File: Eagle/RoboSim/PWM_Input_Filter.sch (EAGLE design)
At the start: 68 parts, among them IC1 LM358, IC2 LM358, IC3 LM358

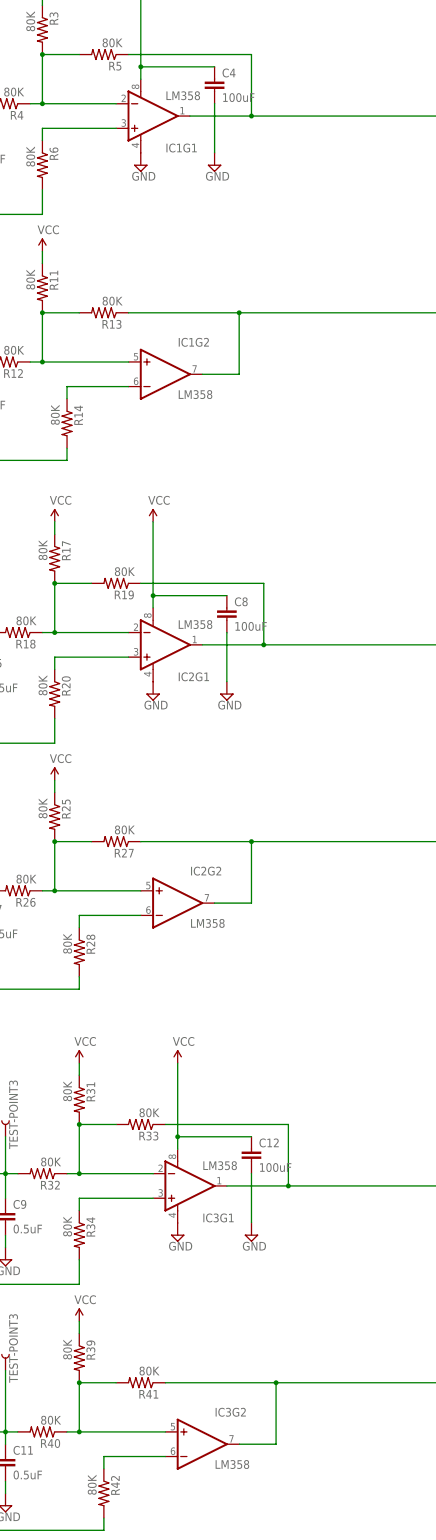
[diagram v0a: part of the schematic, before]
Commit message: updated op amp part number
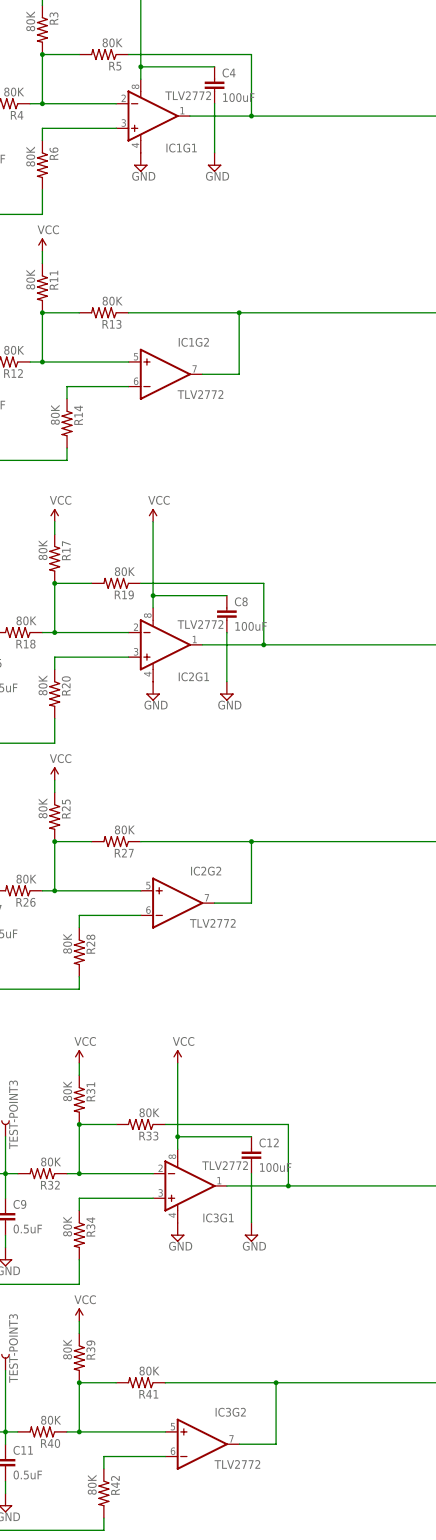
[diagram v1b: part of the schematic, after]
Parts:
- IC1, IC2, IC3: value LM358 -> TLV2772
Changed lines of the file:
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@@
 </classes>
 <parts>
-<part name="IC1" library="SparkFun-AnalogIC" deviceset="LM358" device=""/>
+<part name="IC1" library="SparkFun-AnalogIC" deviceset="LM358" device="" value="TLV2772"/>
 <part name="R1" library="SparkFun-Passives" deviceset="RESISTOR" device="0805-RES" value="80K"/>
 <part name="R2" library="SparkFun-Passives" deviceset="RESISTOR" device="0805-RES" value="20K"/>
@@
 <part name="JP1" library="SparkFun-Connectors" deviceset="M06" device="LOCK"/>
 <part name="JP2" library="SparkFun-Connectors" deviceset="M06" device="LOCK"/>
-<part name="IC2" library="SparkFun-AnalogIC" deviceset="LM358" device=""/>
+<part name="IC2" library="SparkFun-AnalogIC" deviceset="LM358" device="" value="TLV2772"/>
 <part name="R15" library="SparkFun-Passives" deviceset="RESISTOR" device="0805-RES" value="80K"/>
 <part name="R16" library="SparkFun-Passives" deviceset="RESISTOR" device="0805-RES" value="20K"/>
@@
 <part name="C8" library="SparkFun-Passives" deviceset="CAP" device="PTH" value="100uF"/>
 <part name="SUPPLY28" library="supply2" deviceset="GND" device=""/>
-<part name="IC3" library="SparkFun-AnalogIC" deviceset="LM358" device=""/>
+<part name="IC3" library="SparkFun-AnalogIC" deviceset="LM358" device="" value="TLV2772"/>
 <part name="R29" library="SparkFun-Passives" deviceset="RESISTOR" device="0805-RES" value="80K"/>
 <part name="R30" library="SparkFun-Passives" deviceset="RESISTOR" device="0805-RES" value="20K"/>

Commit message: Updated pwm input filter schematic
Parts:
- removed C10, C12: 100uF, SparkFun-Passives:CAPPTH
- removed C11: 0.5uF, SparkFun-Passives:CAPPTH
- removed TP1, TP2, TP3, TP4, TP5, TP6: TEST-POINT3, SparkFun-Passives:TEST-POINT3
- added JP4: (no value), SparkFun-Connectors:M06LOCK
- added R43, R44: 10K, SparkFun-Passives:RESISTORPTH-1/4W
- added R45, R46, R47, R48: 4.7K, SparkFun-Passives:RESISTORPTH-1/4W
- C1, C3, C5, C7, C9: value 0.5uF -> 100uF
- R1, R11, R12, R17, R18, R19, R20, R25, R26, R27, R28, R3, R33, R34, R35, R36, R4, R41, R42, R9: value 80K -> 10K; device SparkFun-Passives:RESISTOR0805-RES -> SparkFun-Passives:RESISTORPTH-1/4W
- R10, R2: value 20K -> 10K; device SparkFun-Passives:RESISTOR0805-RES -> SparkFun-Passives:RESISTORPTH-1/4W
- R13, R14, R15, R21, R22, R23, R29, R31, R32, R37, R39, R40, R5, R6, R7, R8: value 80K -> 4.7K; device SparkFun-Passives:RESISTOR0805-RES -> SparkFun-Passives:RESISTORPTH-1/4W
- R16, R24, R30, R38: value 20K -> 4.7K; device SparkFun-Passives:RESISTOR0805-RES -> SparkFun-Passives:RESISTORPTH-1/4W
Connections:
- removed net N$4: IC1G1.OUT, JP2.1, R5.1
- new net N$18: C6.1, IC2G2.OUT, JP2.4, R30.2
- new net N$19: JP4.6, R26.2
- new net N$23: IC2G1.+IN, R17.1, R20.2, R23.2
- new net N$24: R21.2, R22.1
- new net N$29: R31.1, R32.2
- new net N$34: JP4.2, R42.2
- new net N$35: JP4.1, R41.2
- new net N$43: R47.1, R48.2
- new net N$44: C1.1, IC1G1.OUT, JP2.1, R6.2
- new net N$6: IC1G1.-IN, R1.1, R3.2, R5.1
- net GND: now also R32.1, R40.1, R48.1; no longer C10.2, C11.2, C12.2, R10.1, R2.1, R22.1, R30.1, R36.1, R38.1
- net N$10: now also R7.1, R8.2; no longer IC1G2.+IN, R11.2, R12.1, R13.2
- net N$11: now also IC1G2.+IN, R10.1, R11.2, R13.1; no longer C2.1, R14.2, R6.2, R7.1, R8.2
- net N$12: now also R12.2, R15.2, R9.1; no longer R14.1
- net N$13: now also C3.1, R14.2; no longer R13.1
- net N$14: now also R10.2; no longer R15.2
- net N$15: now also R13.2, R14.1; no longer C5.1, R15.1, R16.2, R18.2, TP3.1
- net N$16: now also JP1.1, R17.2; no longer IC2G1.OUT, JP2.3, R19.1
- net N$17: now also R15.1, R16.2; no longer IC2G1.-IN, R17.2, R18.1, R19.2
- net N$2: now also JP1.2, R18.2; no longer C1.1, R1.1, R2.2, R4.2, TP1.1
- net N$20: now also JP4.5, R25.2; no longer IC2G1.+IN, R20.1
- net N$21: now also R9.2; no longer R23.2
- net N$22: now also IC2G1.-IN, R18.1, R19.2, R21.1; no longer C7.1, R23.1, R24.2, R26.2, TP4.1
- net N$25: now also R23.1, R24.2; no longer IC2G2.+IN, R25.2, R26.1, R27.2
- net N$26: now also IC2G2.+IN, R26.1, R27.2, R29.1; no longer C6.1, R20.2, R21.1, R22.2, R28.2
- net N$27: now also IC2G2.-IN, R25.1, R28.2, R31.2; no longer IC3G1.OUT, JP2.5, R33.1
- net N$28: now also R29.2, R30.1; no longer IC2G2.-IN, R28.1
- net N$3: now also C5.1, IC2G1.OUT, JP2.3, R22.2; no longer IC1G1.-IN, R3.2, R4.1, R5.2
- net N$30: now also JP4.4, R34.2; no longer IC2G2.OUT, JP2.4, R27.1
- net N$31: now also C8.1, IC3G1.OUT, JP2.5, R38.2; no longer JP1.2, R29.2
- net N$32: now also JP4.3, R33.2; no longer C9.1, R29.1, R30.2, R32.2, TP5.1
- net N$33: now also C9.1, IC3G2.OUT, JP2.6, R46.2; no longer IC3G1.-IN, R31.2, R32.1, R33.2
- net N$36: now also IC3G1.-IN, R35.2, R37.1; no longer IC3G1.+IN
- net N$37: now also IC3G1.+IN, R33.1, R36.2, R39.2; no longer JP1.1, R37.2
- net N$38: now also R37.2, R38.1; no longer C11.1, R37.1, R38.2, R40.2, TP6.1
- net N$39: now also R39.1, R40.2; no longer IC3G2.+IN, R39.2, R40.1, R41.2
- net N$40: now also IC3G2.+IN, R42.1, R43.2, R45.1; no longer C10.1, R34.2, R35.1, R36.2, R42.2
- net N$41: now also R41.1, R44.2, R47.2; no longer R42.1
- net N$42: now also R45.2, R46.1; no longer IC3G2.OUT, JP2.6, R41.1
- net N$7: now also R2.1, R4.2, R7.2; no longer R6.1
- net N$8: now also R2.2; no longer R9.2
- net N$9: now also R5.2, R6.1; no longer C3.1, R10.2, R12.2, R9.1, TP2.1
- net VCC: now also C2.1, C7.1, R12.1, R19.1, R20.1, R27.1, R28.1, R35.1, R36.1, R4.1, R43.1, R44.1; no longer C12.1, C8.1, R17.1, R21.2, R25.1, R31.1, R35.2, R39.1, R7.2
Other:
- moved on the sheet: C1, C2, C3, C4, C5, C6, C7, C8, C9, IC1G1, IC1G2, IC2G1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

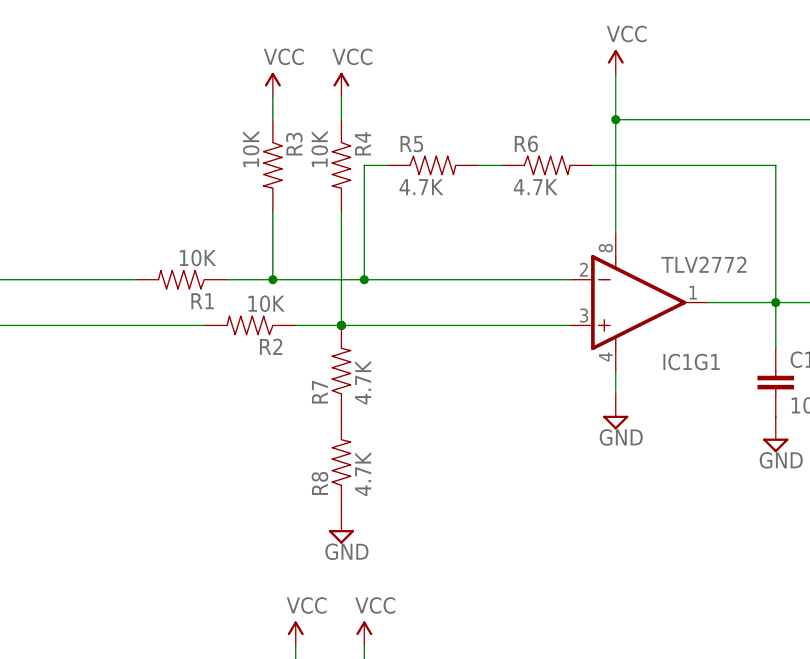
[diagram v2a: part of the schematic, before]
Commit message: updated circuit 1 on the board to proper experimented values. Need to update the others as well
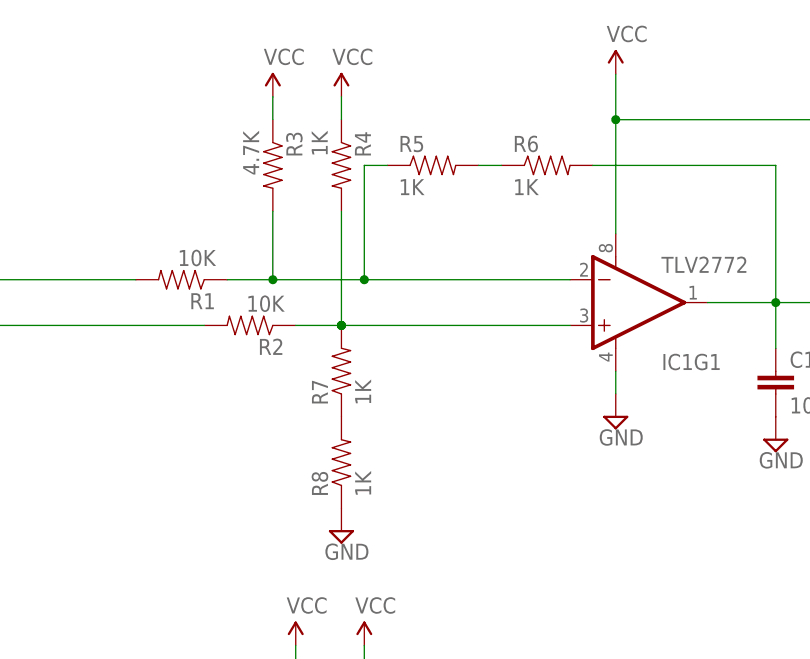
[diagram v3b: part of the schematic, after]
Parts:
- R3: value 10K -> 4.7K
- R4: value 10K -> 1K
- R5, R6, R7, R8: value 4.7K -> 1K
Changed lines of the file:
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@@
 <?xml version="1.0" encoding="utf-8"?>
 <!DOCTYPE eagle SYSTEM "eagle.dtd">
-<eagle version="6.5.0">
+<eagle version="7.3.0">
 <drawing>
 <settings>
@@
 <grid distance="0.1" unitdist="inch" unit="inch" style="lines" multiple="1" display="no" altdistance="0.01" altunitdist="inch" altunit="inch"/>
 <layers>
-<layer number="1" name="Top" color="4" fill="1" visible="yes" active="no"/>
-<layer number="16" name="Bottom" color="1" fill="1" visible="yes" active="no"/>
-<layer number="17" name="Pads" color="2" fill="1" visible="yes" active="no"/>
-<layer number="18" name="Vias" color="2" fill="1" visible="yes" active="no"/>
-<layer number="19" name="Unrouted" color="6" fill="1" visible="yes" active="no"/>
-<layer number="20" name="Dimension" color="15" fill="1" visible="yes" active="no"/>
-<layer number="21" name="tPlace" color="7" fill="1" visible="yes" active="no"/>
-<layer number="22" name="bPlace" color="7" fill="1" visible="yes" active="no"/>
-<layer number="23" name="tOrigins" color="15" fill="1" visible="yes" active="no"/>
-<layer number="24" name="bOrigins" color="15" fill="1" visible="yes" active="no"/>
-<layer number="25" name="tNames" color="7" fill="1" visible="yes" active="no"/>
-<layer number="26" name="bNames" color="7" fill="1" visible="yes" active="no"/>
-<layer number="27" name="tValues" color="7" fill="1" visible="yes" active="no"/>
-<layer number="28" name="bValues" color="7" fill="1" visible="yes" active="no"/>
+<layer number="1" name="Top" color="4" fill="1" visible="no" active="no"/>
+<layer number="16" name="Bottom" color="1" fill="1" visible="no" active="no"/>
+<layer number="17" name="Pads" color="2" fill="1" visible="no" active="no"/>
+<layer number="18" name="Vias" color="2" fill="1" visible="no" active="no"/>
+<layer number="19" name="Unrouted" color="6" fill="1" visible="no" active="no"/>
+<layer number="20" name="Dimension" color="15" fill="1" visible="no" active="no"/>
+<layer number="21" name="tPlace" color="7" fill="1" visible="no" active="no"/>
+<layer number="22" name="bPlace" color="7" fill="1" visible="no" active="no"/>
+<layer number="23" name="tOrigins" color="15" fill="1" visible="no" active="no"/>
+<layer number="24" name="bOrigins" color="15" fill="1" visible="no" active="no"/>
+<layer number="25" name="tNames" color="7" fill="1" visible="no" active="no"/>
+<layer number="26" name="bNames" color="7" fill="1" visible="no" active="no"/>
+<layer number="27" name="tValues" color="7" fill="1" visible="no" active="no"/>
+<layer number="28" name="bValues" color="7" fill="1" visible="no" active="no"/>
 <layer number="29" name="tStop" color="7" fill="3" visible="no" active="no"/>
 <layer number="30" name="bStop" color="7" fill="6" visible="no" active="no"/>
@@
 <layer number="35" name="tGlue" color="7" fill="4" visible="no" active="no"/>
 <layer number="36" name="bGlue" color="7" fill="5" visible="no" active="no"/>
-<layer number="37" name="tTest" color="7" fill="1" visible="yes" active="no"/>
-<layer number="38" name="bTest" color="7" fill="1" visible="yes" active="no"/>
+<layer number="37" name="tTest" color="7" fill="1" visible="no" active="no"/>
+<layer number="38" name="bTest" color="7" fill="1" visible="no" active="no"/>
 <layer number="39" name="tKeepout" color="4" fill="11" visible="no" active="no"/>
 <layer number="40" name="bKeepout" color="1" fill="11" visible="no" active="no"/>
@@
 <layer number="44" name="Drills" color="7" fill="1" visible="no" active="no"/>
 <layer number="45" name="Holes" color="7" fill="1" visible="no" active="no"/>
-<layer number="46" name="Milling" color="3" fill="1" visible="yes" active="no"/>
-<layer number="47" name="Measures" color="7" fill="1" visible="yes" active="no"/>
-<layer number="48" name="Document" color="7" fill="1" visible="yes" active="no"/>
-<layer number="49" name="Reference" color="7" fill="1" visible="yes" active="no"/>
-<layer number="50" name="dxf" color="7" fill="1" visible="yes" active="no"/>
-<layer number="51" name="tDocu" color="7" fill="1" visible="yes" active="no"/>
-<layer number="52" name="bDocu" color="7" fill="1" visible="yes" active="no"/>
-<layer number="53" name="tGND_GNDA" color="7" fill="9" visible="yes" active="no"/>
-<layer number="54" name="bGND_GNDA" color="1" fill="9" visible="yes" active="no"/>
-<layer number="56" name="wert" color="7" fill="1" visible="yes" active="no"/>
+<layer number="46" name="Milling" color="3" fill="1" visible="no" active="no"/>
+<layer number="47" name="Measures" color="7" fill="1" visible="no" active="no"/>
+<layer number="48" name="Document" color="7" fill="1" visible="no" active="no"/>
+<layer number="49" name="Reference" color="7" fill="1" visible="no" active="no"/>
+<layer number="50" name="dxf" color="7" fill="1" visible="no" active="no"/>
+<layer number="51" name="tDocu" color="7" fill="1" visible="no" active="no"/>
+<layer number="52" name="bDocu" color="7" fill="1" visible="no" active="no"/>
+<layer number="53" name="tGND_GNDA" color="7" fill="9" visible="no" active="no"/>
+<layer number="54" name="bGND_GNDA" color="1" fill="9" visible="no" active="no"/>
+<layer number="56" name="wert" color="7" fill="1" visible="no" active="no"/>
 <layer number="91" name="Nets" color="2" fill="1" visible="yes" active="yes"/>
 <layer number="92" name="Busses" color="1" fill="1" visible="yes" active="yes"/>
@@
 <part name="R2" library="SparkFun-Passives" deviceset="RESISTOR" device="PTH-1/4W" value="10K"/>
 <part name="R1" library="SparkFun-Passives" deviceset="RESISTOR" device="PTH-1/4W" value="10K"/>
-<part name="R3" library="SparkFun-Passives" deviceset="RESISTOR" device="PTH-1/4W" value="10K"/>
+<part name="R3" library="SparkFun-Passives" deviceset="RESISTOR" device="PTH-1/4W" value="4.7K"/>
 <part name="SUPPLY4" library="SparkFun-Aesthetics" deviceset="VCC" device=""/>
-<part name="R4" library="SparkFun-Passives" deviceset="RESISTOR" device="PTH-1/4W" value="10K"/>
+<part name="R4" library="SparkFun-Passives" deviceset="RESISTOR" device="PTH-1/4W" value="1K"/>
 <part name="SUPPLY5" library="supply2" deviceset="GND" device=""/>
 <part name="C1" library="SparkFun-Passives" deviceset="CAP" device="PTH" value="100uF"/>
 <part name="SUPPLY6" library="supply2" deviceset="GND" device=""/>
-<part name="R5" library="SparkFun-Passives" deviceset="RESISTOR" device="PTH-1/4W" value="4.7K"/>
-<part name="R6" library="SparkFun-Passives" deviceset="RESISTOR" device="PTH-1/4W" value="4.7K"/>
-<part name="R7" library="SparkFun-Passives" deviceset="RESISTOR" device="PTH-1/4W" value="4.7K"/>
-<part name="R8" library="SparkFun-Passives" deviceset="RESISTOR" device="PTH-1/4W" value="4.7K"/>
+<part name="R5" library="SparkFun-Passives" deviceset="RESISTOR" device="PTH-1/4W" value="1K"/>
+<part name="R6" library="SparkFun-Passives" deviceset="RESISTOR" device="PTH-1/4W" value="1K"/>
+<part name="R7" library="SparkFun-Passives" deviceset="RESISTOR" device="PTH-1/4W" value="1K"/>
+<part name="R8" library="SparkFun-Passives" deviceset="RESISTOR" device="PTH-1/4W" value="1K"/>
 <part name="SUPPLY10" library="supply2" deviceset="GND" device=""/>
 <part name="SUPPLY11" library="supply2" deviceset="GND" device=""/>
